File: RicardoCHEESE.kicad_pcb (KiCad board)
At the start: 4 copper layers, 143 parts, among them IC1 SiC437BED-T1-GE3, J1 RBUS, J2 USB_C_Receptacle_USB2.0, J3 Conn_Coaxial, J4 Conn_01x06_Pin, J5 Conn_01x06_Pin, J6 Conn_01x06_Pin, J7 Conn_01x06_Pin, J8 Conn_01x02_Male, U1 ESP32-S3, U2 SN65HVD230, U3 LM66200DRLR, U4 SC4215, U5 MAX77827AEFD+T, U6 SE5005L, U7 RTC6705, U8 HEF4051BT, Y1 40MHz±10ppm, Y2 8MHz

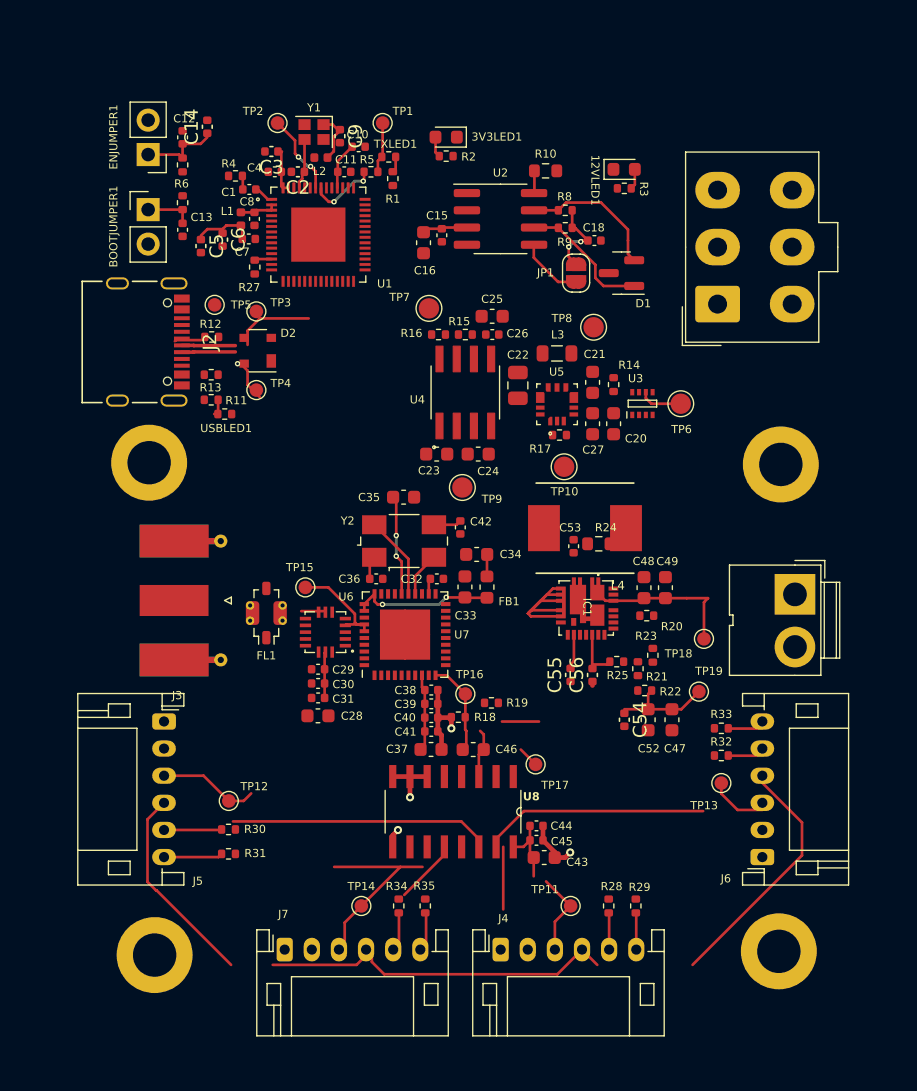
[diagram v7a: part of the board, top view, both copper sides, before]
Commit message: Footprinting and board outline
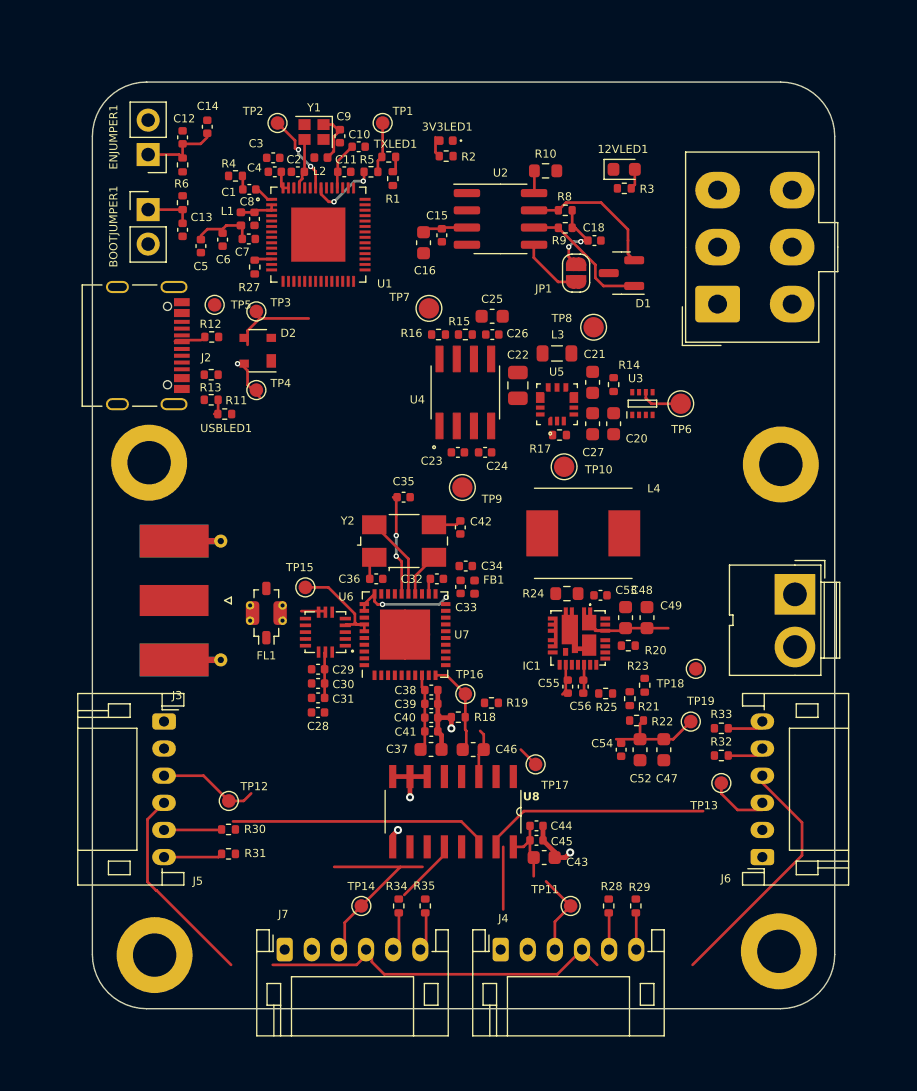
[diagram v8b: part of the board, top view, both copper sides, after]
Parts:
- 3V3LED1: footprint LED_SMD:LED_0603_1608Metric -> LED_SMD:LED_0402_1005Metric
- C23, C24, C28, C33, C34, C35: footprint Capacitor_SMD:C_0603_1608Metric -> Capacitor_SMD:C_0402_1005Metric
- FB1: footprint Inductor_SMD:L_0603_1608Metric -> Inductor_SMD:L_0402_1005Metric
- moved R24 4.36 mm to (146.2, 98.3), turned to 0 degrees
- moved C53 4.13 mm to (148.6, 98.4), turned to 180 degrees
- moved C49 2.60 mm to (152.1, 100.1)
- moved R20 2.60 mm to (150.7, 102.2)
- moved C48 2.60 mm to (150.5, 100.1)
- moved R25 2.49 mm to (149.0, 105.7)
- moved IC1 2.29 mm to (147.0, 101.6)
- moved R21 2.29 mm to (150.8, 106.1)
- moved R22 2.29 mm to (151.3, 107.7)
- moved TP18 2.29 mm to (155.7, 103.9)
- moved TP19 2.29 mm to (155.3, 107.8)
- moved C47 2.29 mm to (153.3, 109.8)
- moved C52 2.29 mm to (151.6, 109.8)
- moved R23 2.29 mm to (151.9, 105.1)
- moved C54 2.22 mm to (150.2, 109.8)
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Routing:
- net Net-(IC1-SW_1): track 13.3 -> 0.00 mm
- net Net-(IC1-VIN_1): track 11.6 -> 6.92 mm
- net /Data-: track 9.88 -> 5.93 mm
- net /Data+: track 7.22 -> 3.27 mm
- net +3.3V: track 25.0 -> 21.9 mm
- net +3.3VA: track 11.9 -> 8.88 mm
- net Net-(U8-Z): track 7.91 -> 5.17 mm
- net Net-(IC1-VDD): track 3.56 -> 2.20 mm
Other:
- board outline added: 54.7 x 68.3 mm
